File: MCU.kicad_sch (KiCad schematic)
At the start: 13 parts, among them U4 EFM32GG332

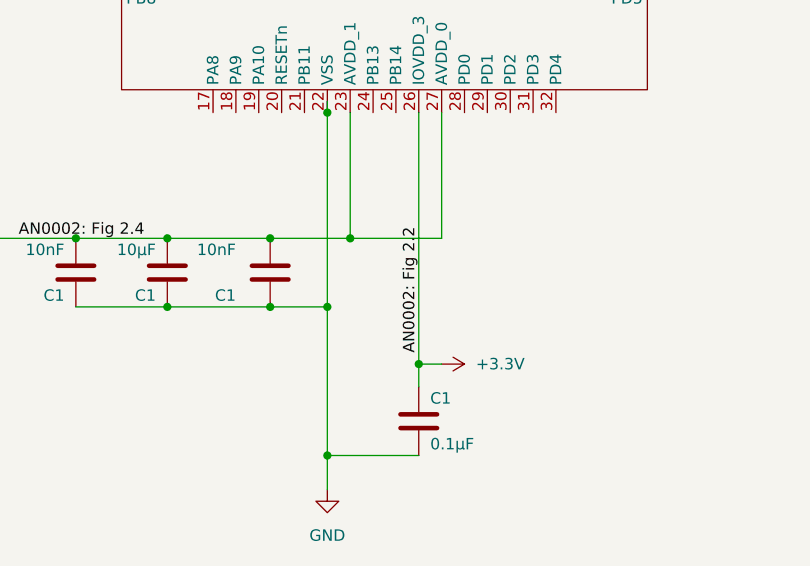
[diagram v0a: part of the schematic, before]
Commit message: Changed label to text
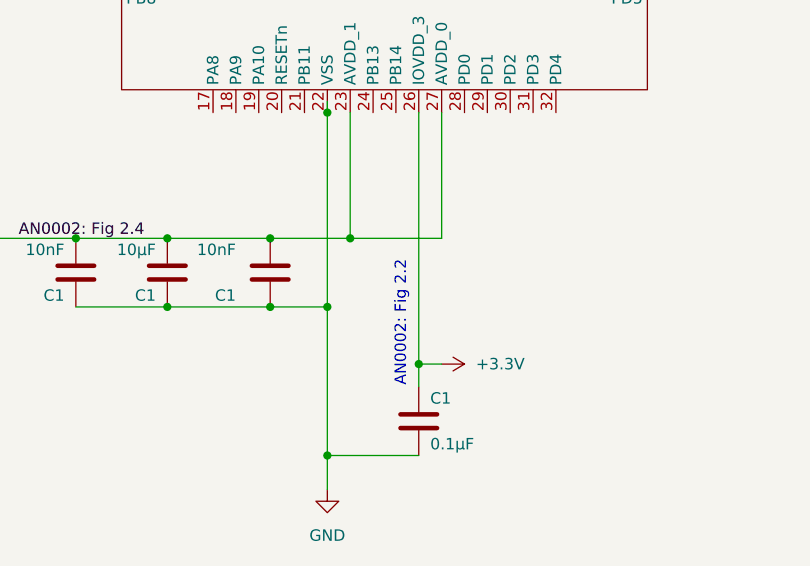
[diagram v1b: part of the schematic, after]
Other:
- note added: "AN0002: Fig 2.2"
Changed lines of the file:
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@@
     (stroke (width 0) (type default))
+  )
+  (text "AN0002: Fig 2.2" (at 140.97 149.86 90)
+    (effects (font (size 1.27 1.27)) (justify left bottom))
   )
   (text "AN0002: Fig 2.1" (at 193.04 91.44 0)
     (effects (font (size 1.27 1.27)) (justify left bottom))
   )
-  (label "AN0002: Fig 2.2" (at 142.24 146.05 90) (fields_autoplaced)
-    (effects (font (size 1.27 1.27)) (justify left bottom))
-  )

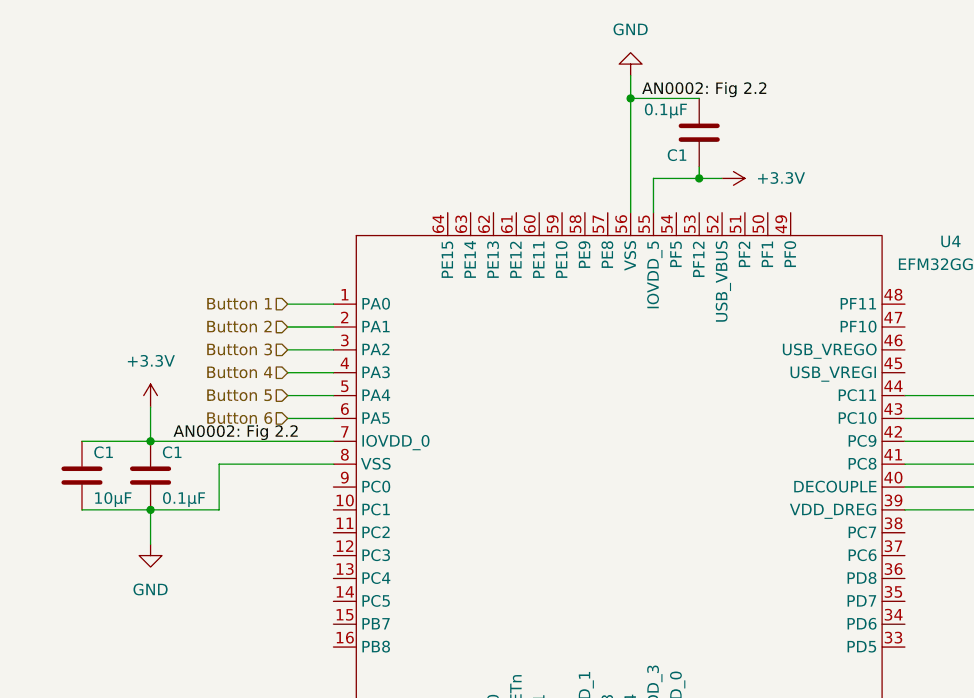
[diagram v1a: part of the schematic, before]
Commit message: Connected FPGA and DAC
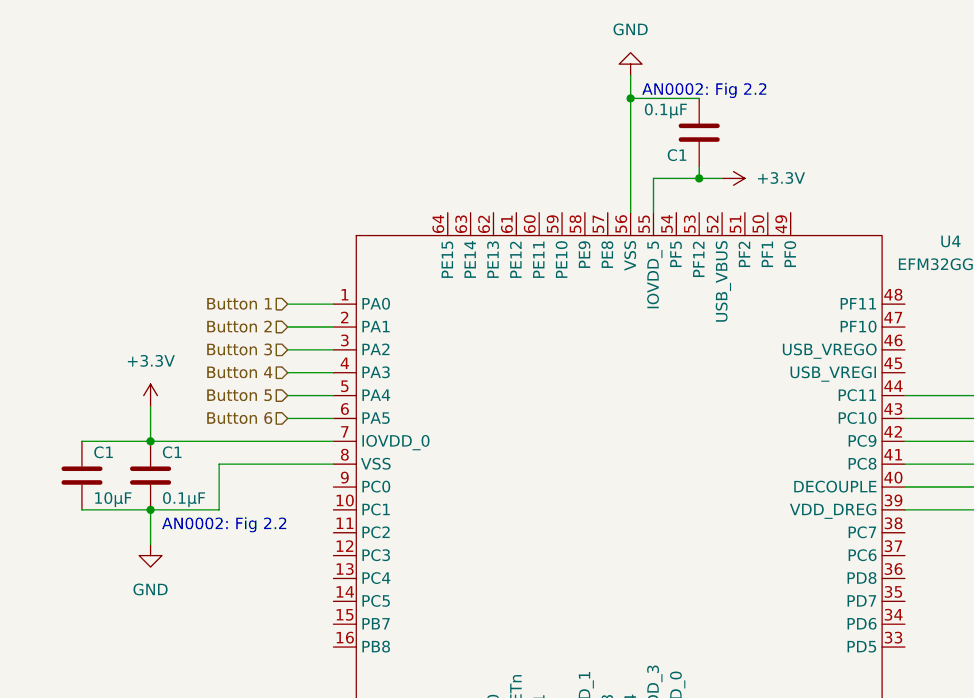
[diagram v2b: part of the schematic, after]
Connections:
- net +3.3V: no longer C1.1, C1.1, C1.1, C1.2, C1.2, C1.2, C1.2, C1.2, C1.2, C4.2, U4.22 (VSS), U4.56 (VSS), U4.8 (VSS)
- new net GND: C1.1, C1.1, C1.1, C1.2, C1.2, C1.2, C1.2, C1.2, C1.2, C4.2, U4.22 (VSS), U4.56 (VSS), U4.8 (VSS)
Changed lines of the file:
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@@
     (effects (font (size 1.27 1.27)) (justify left bottom))
   )
-  (label "AN0002: Fig 2.2" (at 140.97 45.72 0) (fields_autoplaced)
+  (text "AN0002: Fig 2.2" (at 87.63 93.98 0)
     (effects (font (size 1.27 1.27)) (justify left bottom))
   )
-  (label "AN0002: Fig 2.2" (at 88.9 83.82 0) (fields_autoplaced)
+  (text "AN0002: Fig 2.2" (at 140.97 45.72 0)
     (effects (font (size 1.27 1.27)) (justify left bottom))
   )

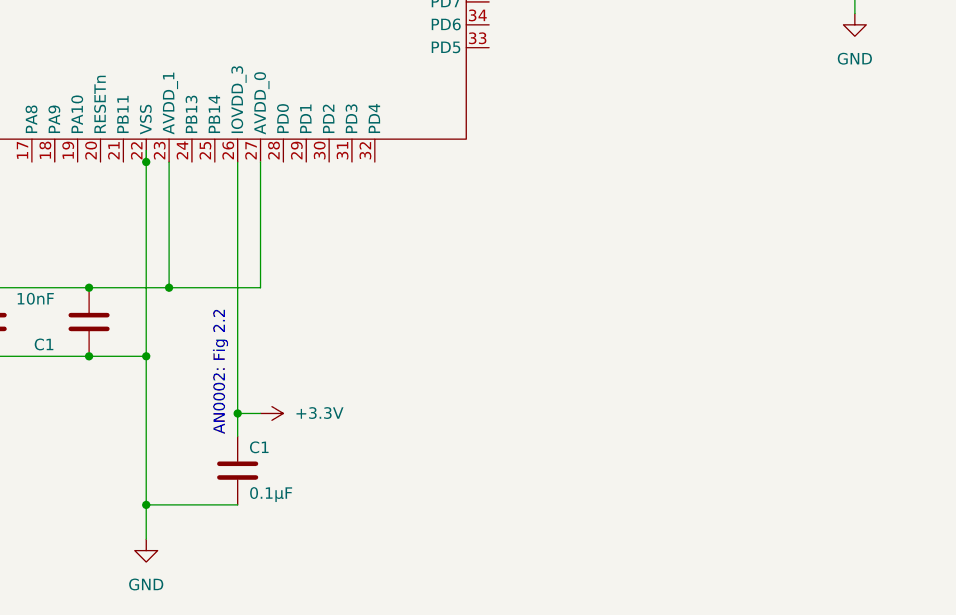
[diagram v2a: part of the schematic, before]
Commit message: Added MCU Crystal for Clock signal
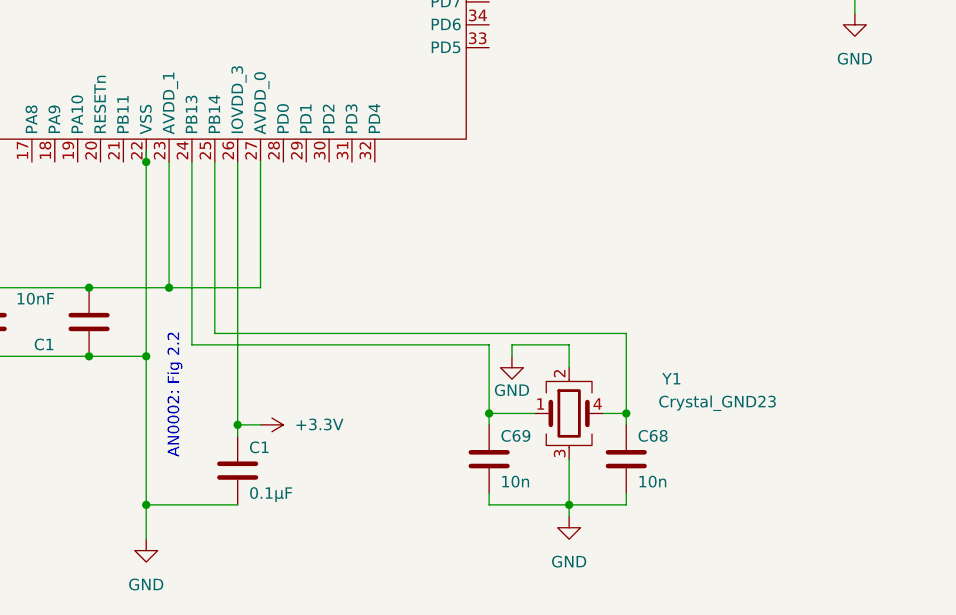
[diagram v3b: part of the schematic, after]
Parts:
- added C68, C69: 10n, symbol Device:C
- added Y1: Crystal_GND23, symbol Device:Crystal_GND23
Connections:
- net GND: now also C68.2, C69.2, Y1.2, Y1.3
- net at U4.24 (PB13): now also C69.1, Y1.1
- net at U4.25 (PB14): now also C68.1, Y1.4

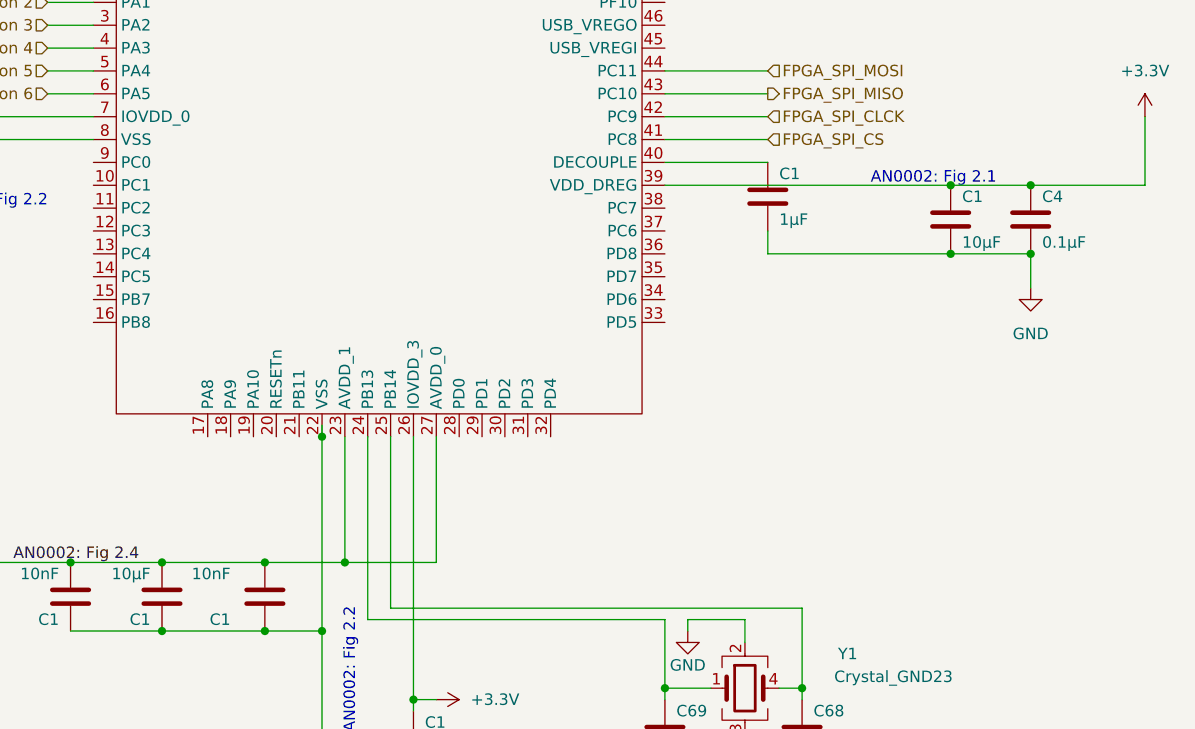
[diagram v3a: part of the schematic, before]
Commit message: Wired FPGA program to MCU
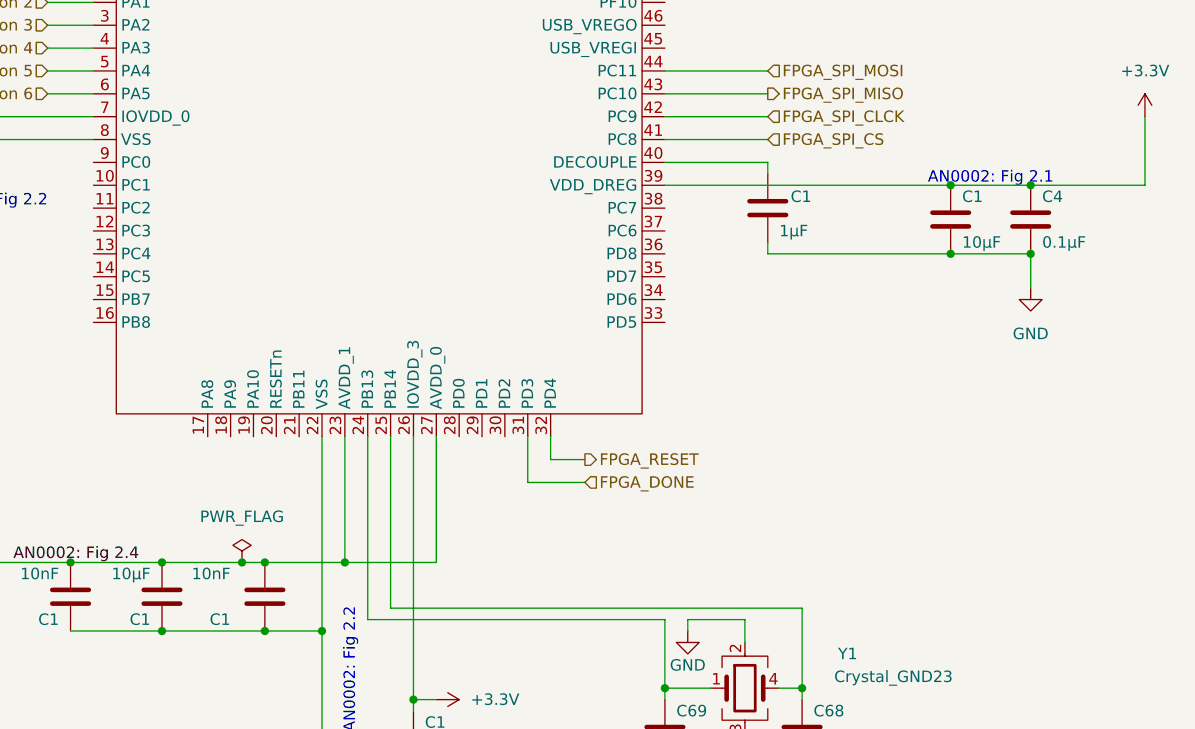
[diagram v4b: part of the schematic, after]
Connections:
- net FPGA_DONE: now reaches U4.31 (PD3)
- net FPGA_RESET: now reaches U4.32 (PD4)
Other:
- moved on the sheet: C1
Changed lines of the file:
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@@
   (junction (at 134.62 133.35) (diameter 0) (color 0 0 0 0)
   )
-  (junction (at 132.08 119.38) (diameter 0) (color 0 0 0 0)
-  )
   (junction (at 210.82 91.44) (diameter 0) (color 0 0 0 0)
   )
@@
   (junction (at 179.07 157.48) (diameter 0) (color 0 0 0 0)
   )
+  (junction (at 123.19 133.35) (diameter 0) (color 0 0 0 0)
+  )
   (wire (pts (xy 185.42 147.32) (xy 182.88 147.32))
     (stroke (width 0) (type default))
@@
     (stroke (width 0) (type default))
   )
+  (wire (pts (xy 132.08 140.97) (xy 132.08 157.48))
+    (stroke (width 0) (type default))
+  )
   (wire (pts (xy 86.36 83.82) (xy 106.68 83.82))
     (stroke (width 0) (type default))
@@
     (stroke (width 0) (type default))
   )
+  (wire (pts (xy 123.19 133.35) (xy 125.73 133.35))
+    (stroke (width 0) (type default))
+  )
   (wire (pts (xy 170.18 157.48) (xy 179.07 157.48))
     (stroke (width 0) (type default))
@@
     (stroke (width 0) (type default))
   )
-  (wire (pts (xy 170.18 88.9) (xy 181.61 88.9))
-    (stroke (width 0) (type default))
-  )
-  (wire (pts (xy 181.61 96.52) (xy 181.61 99.06))
+  (wire (pts (xy 181.61 97.79) (xy 181.61 99.06))
     (stroke (width 0) (type default))
   )
@@
     (stroke (width 0) (type default))
   )
+  (wire (pts (xy 161.29 124.46) (xy 154.94 124.46))
+    (stroke (width 0) (type default))
+  )
+  (wire (pts (xy 161.29 121.92) (xy 157.48 121.92))
+    (stroke (width 0) (type default))
+  )
   (wire (pts (xy 170.18 147.32) (xy 170.18 148.59))
     (stroke (width 0) (type default))
@@
     (stroke (width 0) (type default))
   )
+  (wire (pts (xy 154.94 124.46) (xy 154.94 119.38))
+    (stroke (width 0) (type default))
+  )
+  (wire (pts (xy 157.48 121.92) (xy 157.48 119.38))
+    (stroke (width 0) (type default))
+  )
+  (wire (pts (xy 181.61 90.17) (xy 181.61 88.9))
+    (stroke (width 0) (type default))
+  )
   (wire (pts (xy 93.98 91.44) (xy 86.36 91.44))
     (stroke (width 0) (type default))
@@
     (stroke (width 0) (type default))
   )
+  (wire (pts (xy 181.61 88.9) (xy 170.18 88.9))
+    (stroke (width 0) (type default))
+  )
   (wire (pts (xy 210.82 91.44) (xy 223.52 91.44))
     (stroke (width 0) (type default))
@@
     (stroke (width 0) (type default))
   )
-  (wire (pts (xy 114.3 133.35) (xy 125.73 133.35))
+  (wire (pts (xy 114.3 133.35) (xy 123.19 133.35))
     (stroke (width 0) (type default))
   )
@@
     (stroke (width 0) (type default))
   )
-  (wire (pts (xy 132.08 118.11) (xy 132.08 119.38))
-    (stroke (width 0) (type default))
-  )
   (wire (pts (xy 86.36 95.25) (xy 86.36 91.44))
     (stroke (width 0) (type default))
@@
   )
   (wire (pts (xy 170.18 147.32) (xy 170.18 139.7))
-    (stroke (width 0) (type default))
-  )
-  (wire (pts (xy 132.08 140.97) (xy 132.08 157.48))
     (stroke (width 0) (type default))
   )
@@
     (effects (font (size 1.27 1.27)) (justify left bottom))
   )
-  (text "AN0002: Fig 2.1" (at 193.04 91.44 0)
+  (text "AN0002: Fig 2.1" (at 199.39 91.44 0)
     (effects (font (size 1.27 1.27)) (justify left bottom))
   )
@@
     (effects (font (size 1.27 1.27)) (justify left))
   )
+  (hierarchical_label "FPGA_DONE" (shape input) (at 161.29 124.46 0) (fields_autoplaced)
+    (effects (font (size 1.27 1.27)) (justify left))
+  )
   (hierarchical_label "Button 5" (shape input) (at 101.6 78.74 180) (fields_autoplaced)
     (effects (font (size 1.27 1.27)) (justify right))
@@
   (hierarchical_label "Button 2" (shape input) (at 101.6 71.12 180) (fields_autoplaced)
     (effects (font (size 1.27 1.27)) (justify right))
+  )
+  (hierarchical_label "FPGA_RESET" (shape output) (at 161.29 121.92 0) (fields_autoplaced)
+    (effects (font (size 1.27 1.27)) (justify left))
   )
   (hierarchical_label "Button 3" (shape input) (at 101.6 73.66 180) (fields_autoplaced)
@@
     )
   )
+  (symbol (lib_id "power:PWR_FLAG") (at 123.19 133.35 0) (unit 1)
+    (in_bom yes) (on_board yes) (dnp no) (fields_autoplaced)
+    (property "Reference" "#FLG05" (at 123.19 131.445 0)
+      (effects (font (size 1.27 1.27)) hide)
+    )
+    (property "Value" "PWR_FLAG" (at 123.19 128.27 0)
+      (effects (font (size 1.27 1.27)))
+    )
+    (property "Footprint" "" (at 123.19 133.35 0)
+      (effects (font (size 1.27 1.27)) hide)
+    )
+    (property "Datasheet" "~" (at 123.19 133.35 0)
+      (effects (font (size 1.27 1.27)) hide)
+    )
+    (pin "1")
+    (instances
+      (project "GuitarZero"
+        (path "/fba50eda-8593-4456-af98-ff56fd418a76/ae46c600-e32c-45ef-b9ae-c42d4bac8718"
+          (reference "#FLG05") (unit 1)
+        )
+      )
+    )
+  )
   (symbol (lib_id "Device:C") (at 210.82 95.25 0) (unit 1)
     (in_bom yes) (on_board yes) (dnp no)
@@
     )
   )
-  (symbol (lib_id "Device:C") (at 181.61 92.71 0) (unit 1)
-    (in_bom yes) (on_board yes) (dnp no)
-    (property "Reference" "C1" (at 182.88 90.17 0)
-      (effects (font (size 1.27 1.27)) (justify left))
-    )
-    (property "Value" "1µF" (at 182.88 95.25 0)
-      (effects (font (size 1.27 1.27)) (justify left))
-    )
-    (property "Footprint" "" (at 182.5752 96.52 0)
-      (effects (font (size 1.27 1.27)) hide)
-    )
-    (property "Datasheet" "~" (at 181.61 92.71 0)
-      (effects (font (size 1.27 1.27)) hide)
-    )
+  (symbol (lib_id "Device:C") (at 181.61 93.98 0) (unit 1)
+    (in_bom yes) (on_board yes) (dnp no)
+    (property "Reference" "C1" (at 184.15 92.71 0)
+      (effects (font (size 1.27 1.27)) (justify left))
+    )
+    (property "Value" "1µF" (at 182.88 96.52 0)
+      (effects (font (size 1.27 1.27)) (justify left))
+    )
+    (property "Footprint" "" (at 182.5752 97.79 0)
+      (effects (font (size 1.27 1.27)) hide)
+    )
+    (property "Datasheet" "~" (at 181.61 93.98 0)
+      (effects (font (size 1.27 1.27)) hide)
+    )
